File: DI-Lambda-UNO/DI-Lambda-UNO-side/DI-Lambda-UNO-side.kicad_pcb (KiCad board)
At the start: 2 copper layers, 125 x 28.2 mm, 4 parts, among them J1 CONN_02X04, J2 CONN_02X04, J3 CONN_02X04, J4 CONN_02X04

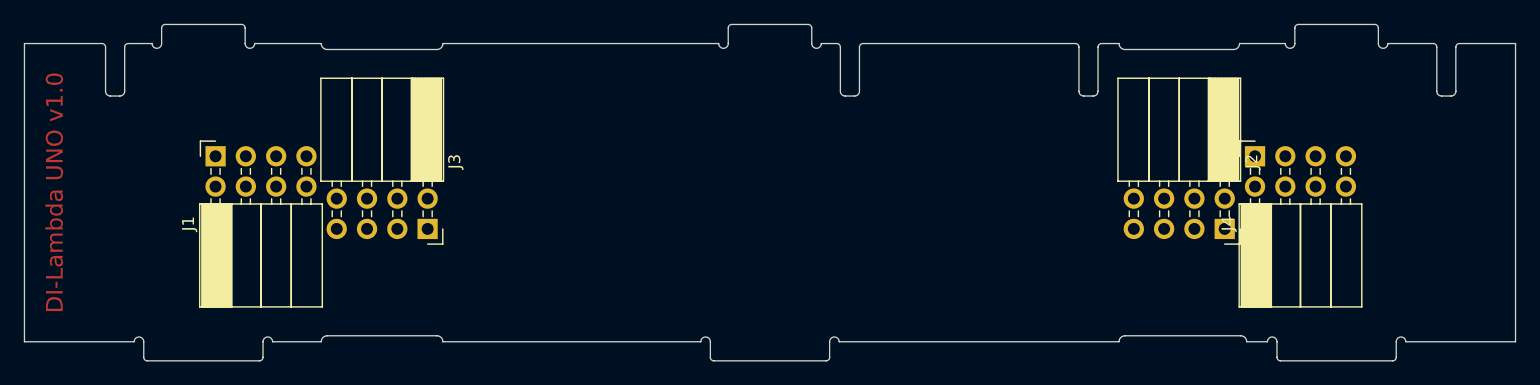
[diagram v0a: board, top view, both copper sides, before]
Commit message: Remove connectors and notches from the side panels
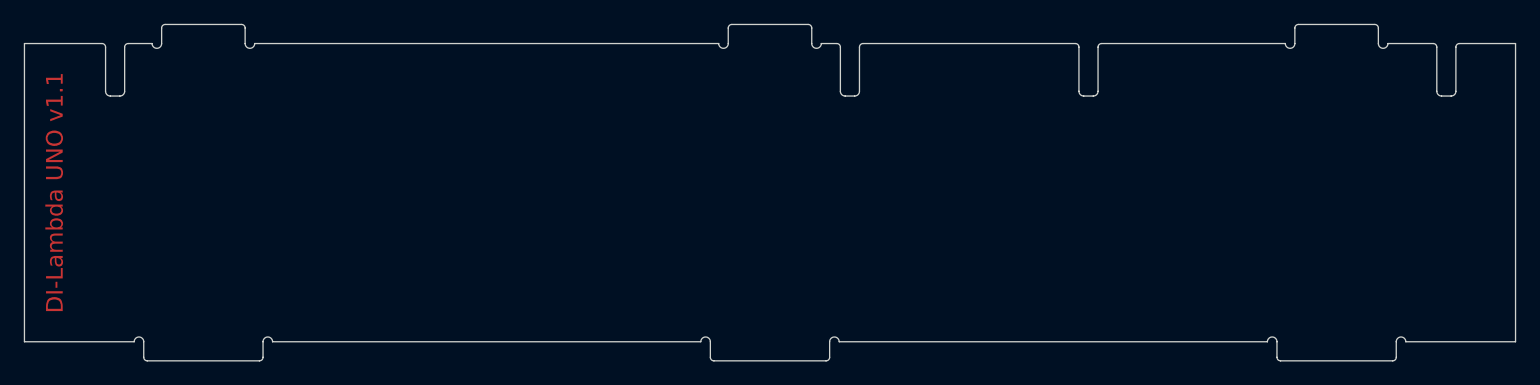
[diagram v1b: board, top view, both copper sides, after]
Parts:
- removed J1, J2, J3, J4: CONN_02X04, Socket_Strips:Socket_Strip_Angled_2x04_Pitch2.54mm
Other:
- outline, holes or cut-outs redrawn
- board text added: "DI-Lambda UNO v1.1"
- board text removed: "DI-Lambda UNO v1.0"
